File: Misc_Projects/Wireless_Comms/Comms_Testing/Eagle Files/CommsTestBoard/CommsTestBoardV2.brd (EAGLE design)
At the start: 100 x 106.7 mm, 21 parts, among them J1 1985205, J2 1985205, U1 XBEE_PRO_S3B, U2 XBEE_PRO_S3B

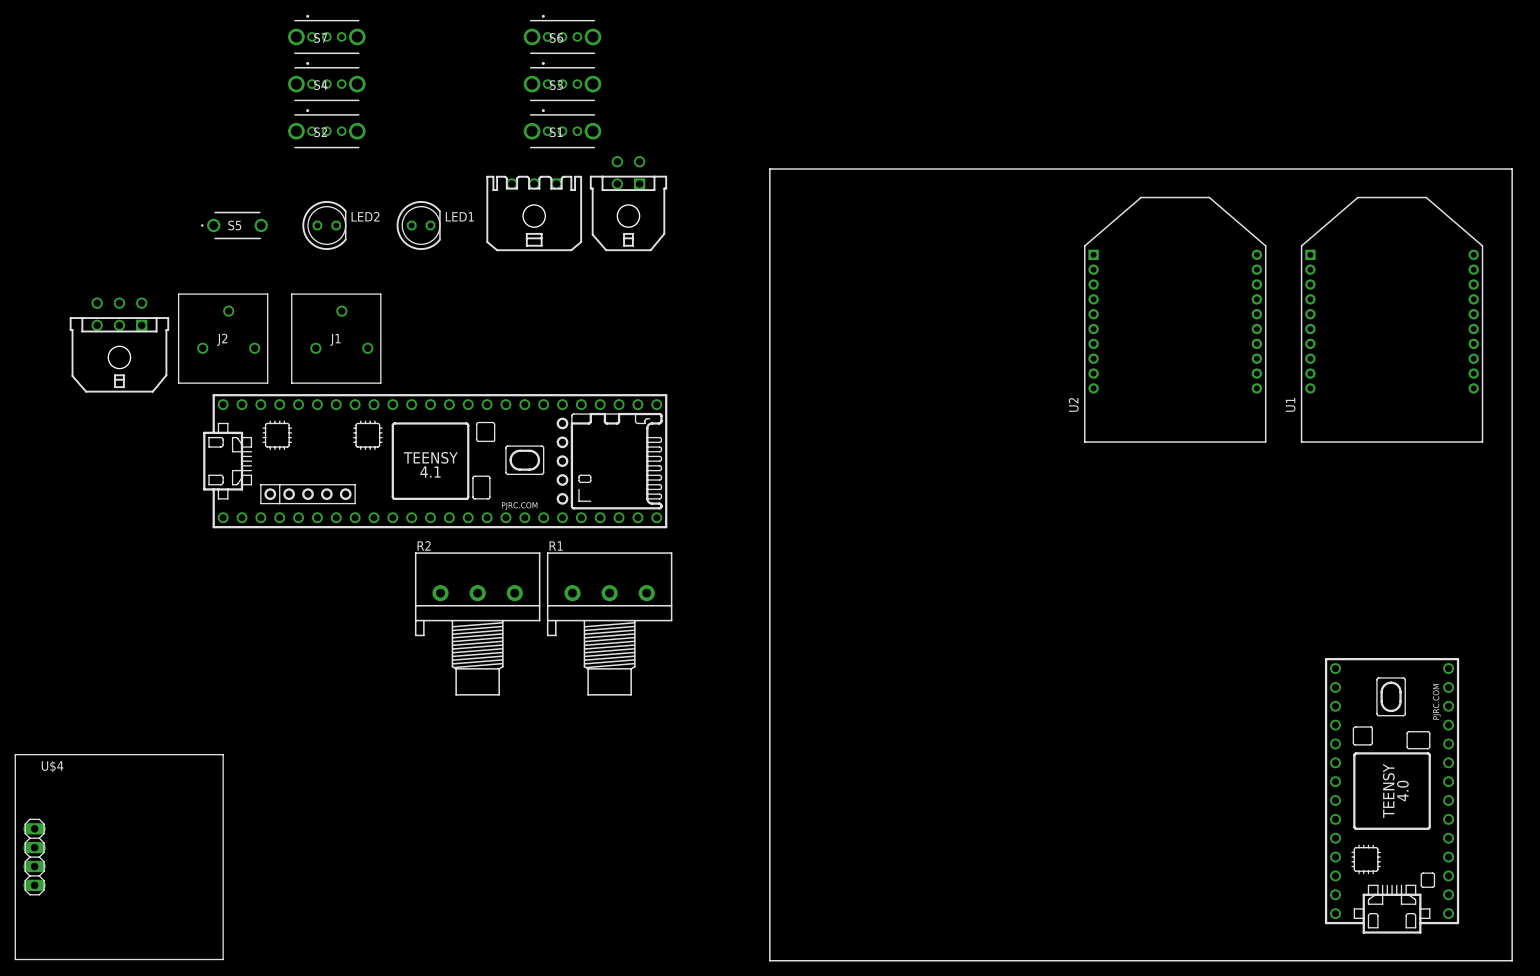
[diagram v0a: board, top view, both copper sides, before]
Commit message: Battery box and commsboardv2 update
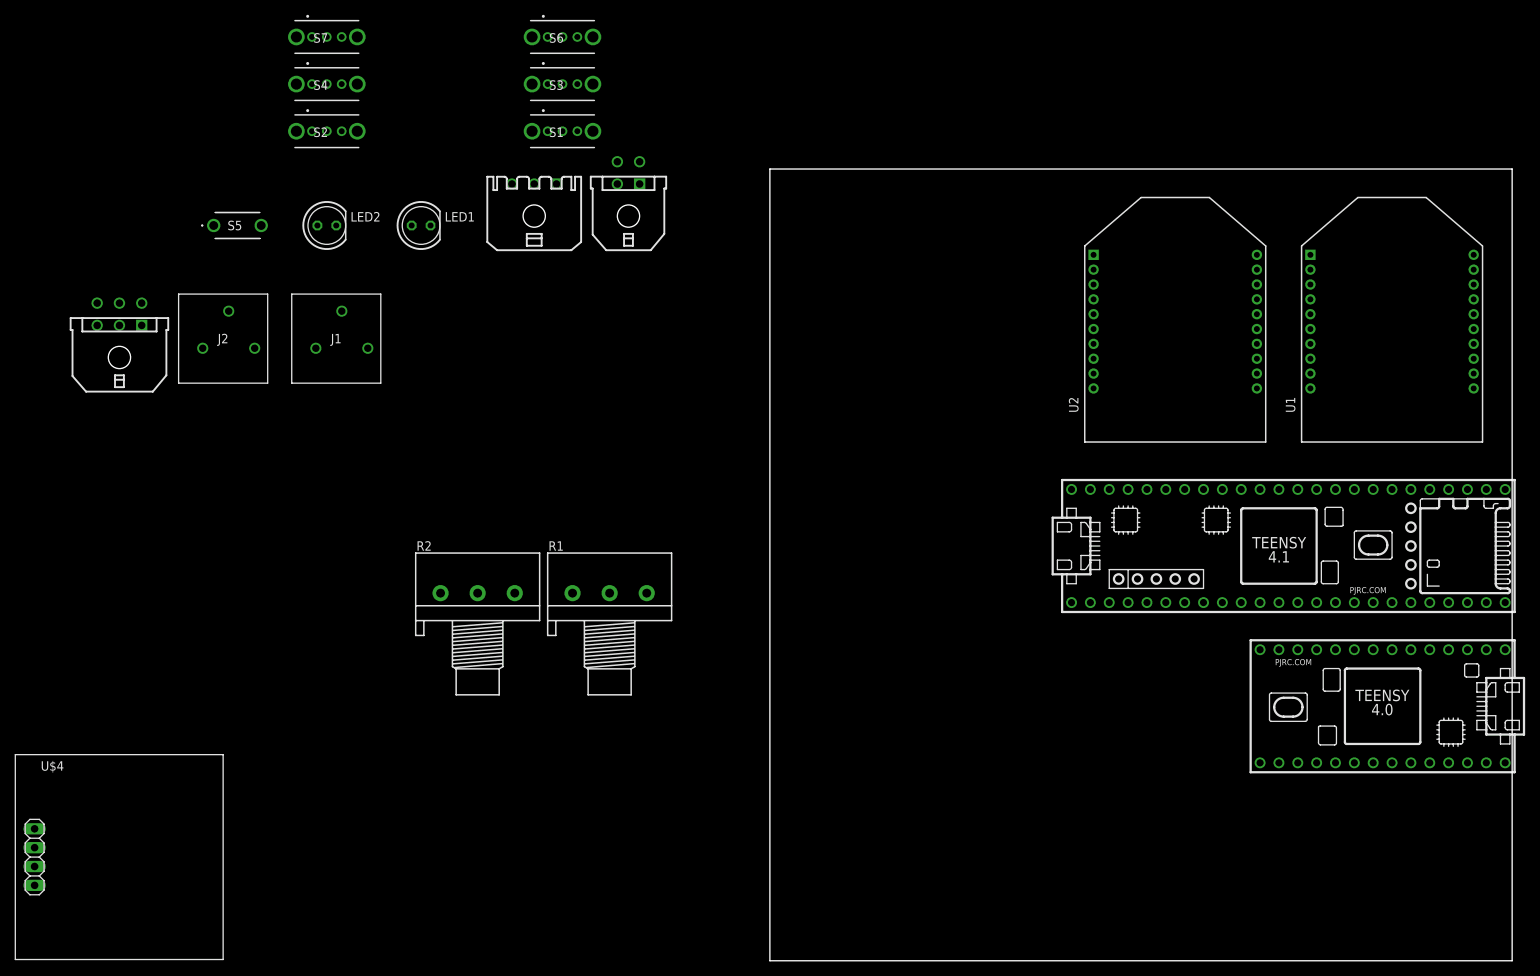
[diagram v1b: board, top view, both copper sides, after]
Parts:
- moved U$3 114.9 mm to (68.6, 55.9)
- moved U$1 11.5 mm to (82.5, 34.3), turned to 180 degrees
